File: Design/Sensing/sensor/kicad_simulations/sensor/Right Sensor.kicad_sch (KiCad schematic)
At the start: 9 parts, among them Q2 2N3904, U2 TSSP58038

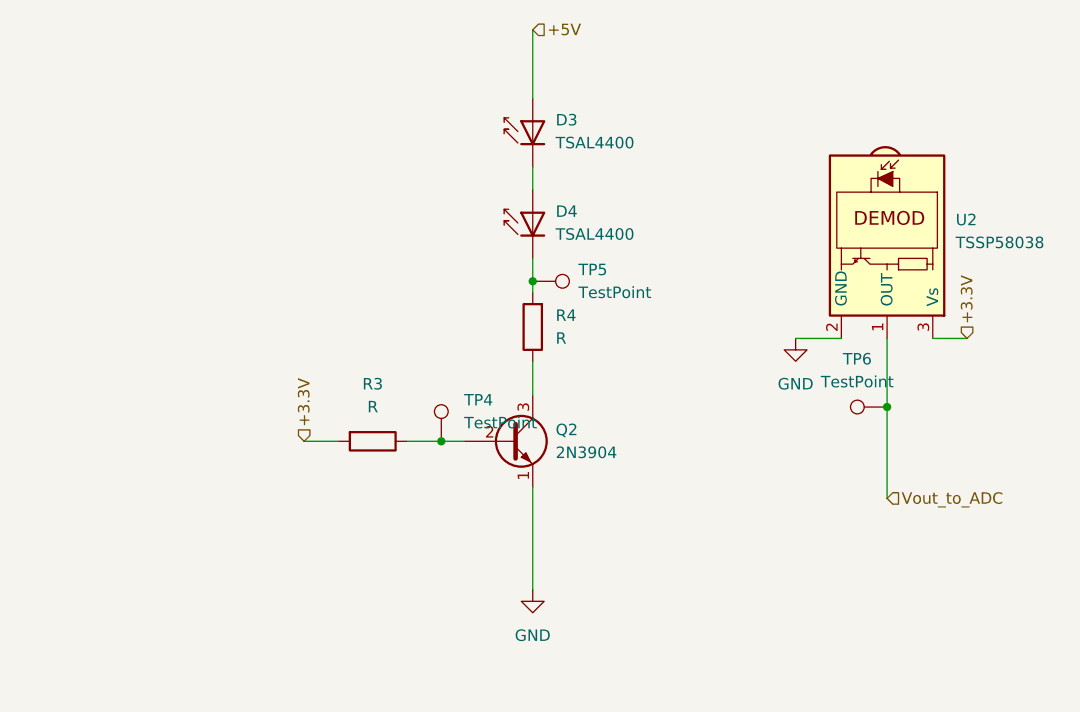
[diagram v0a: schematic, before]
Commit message: Resistor values for emitter circuit done, still have to name the circuits properly
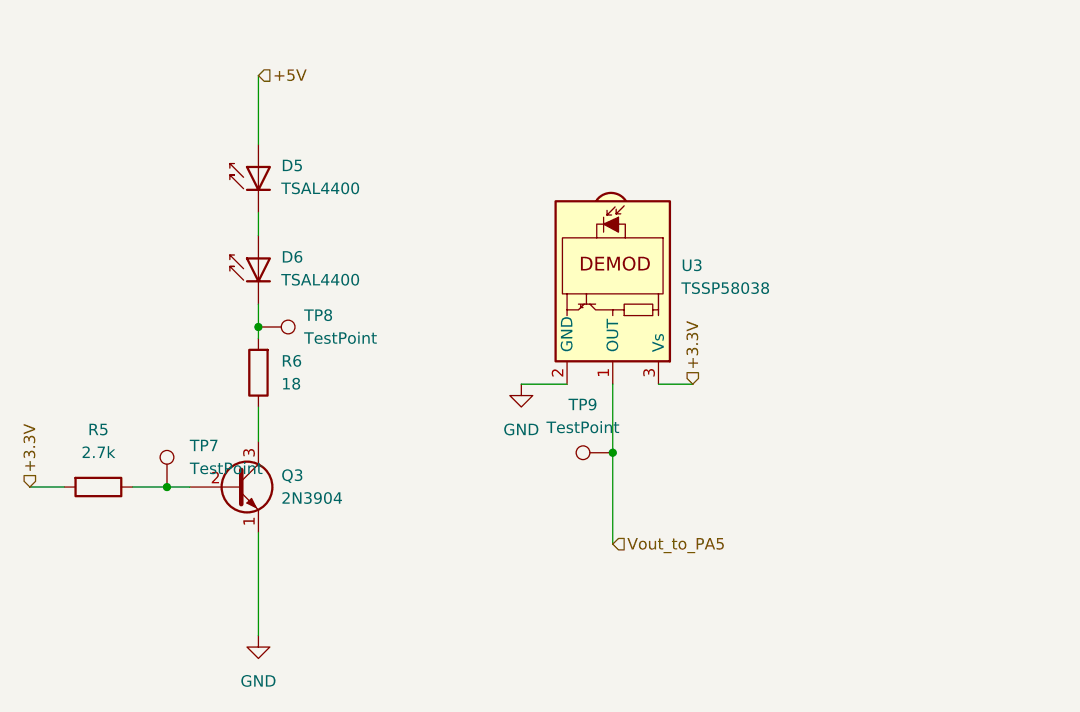
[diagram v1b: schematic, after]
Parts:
- removed D3, D4: TSAL4400, LED_THT:LED_D3.0mm_IRBlack, symbol LED:TSAL4400
- removed Q2: 2N3904, Package_TO_SOT_THT:TO-92_Inline, symbol Transistor_BJT:2N3904
- removed R3, R4: R, symbol Device:R
- removed TP4, TP5, TP6: TestPoint, symbol Connector:TestPoint
- removed U2: TSSP58038, OptoDevice:Vishay_MINICAST-3Pin, symbol Sensor_Proximity:TSSP58038
- added D5, D6: TSAL4400, LED_THT:LED_D3.0mm_IRBlack, symbol LED:TSAL4400
- added Q3: 2N3904, Package_TO_SOT_THT:TO-92_Inline, symbol Transistor_BJT:2N3904
- added R5: 2.7k, symbol Device:R
- added R6: 18, symbol Device:R
- added TP7, TP8, TP9: TestPoint, symbol Connector:TestPoint
- added U3: TSSP58038, OptoDevice:Vishay_MINICAST-3Pin, symbol Sensor_Proximity:TSSP58038
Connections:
- net +3.3V: now also R5.2, U3.3 (Vs)
- net +5V: now also D5.2 (A)
- net GND: now also Q3.1 (E), U3.2 (GND)
- new net: Q3.2 (B), R5.1, TP7.1
- new net: Q3.3 (C), R6.1
- new net: D6.1 (K), R6.2, TP8.1
- new net: D5.1 (K), D6.2 (A)
- new net Vout_to_PA5: TP9.1, U3.1 (OUT)
